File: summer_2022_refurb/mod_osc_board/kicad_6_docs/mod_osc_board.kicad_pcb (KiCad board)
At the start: 2 copper layers, 123.2 x 76.2 mm, 112 parts, among them J1 ext_port, J2 ribbon_board_port, J3 adsr_board_port, J4 vco_board_port, J5 vcf_board_port, J6 power_entry, SW101 SW_SPDT_MSM, SW201 alpha_SR2612F-0112, U201 SSI2130, U202 TL072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

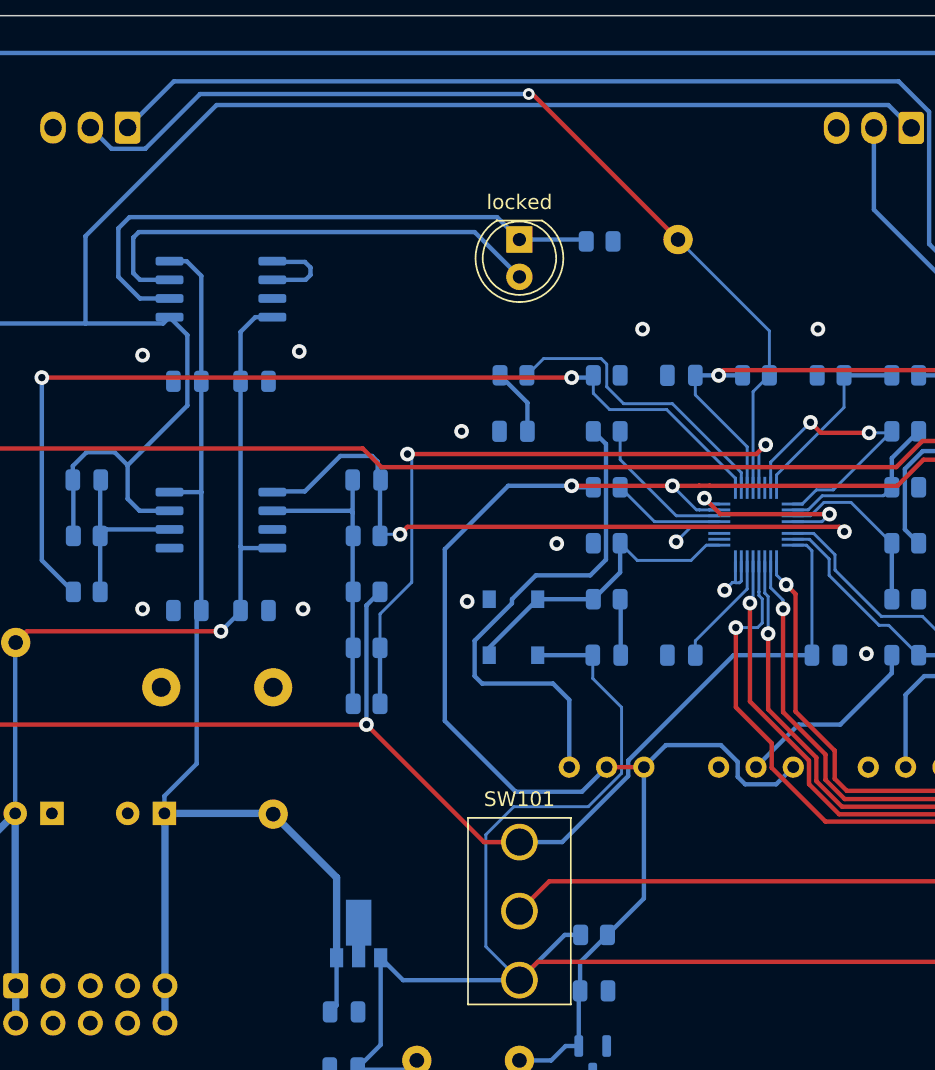
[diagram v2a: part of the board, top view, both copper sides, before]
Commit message: Buffer square, add saw polarity jumper
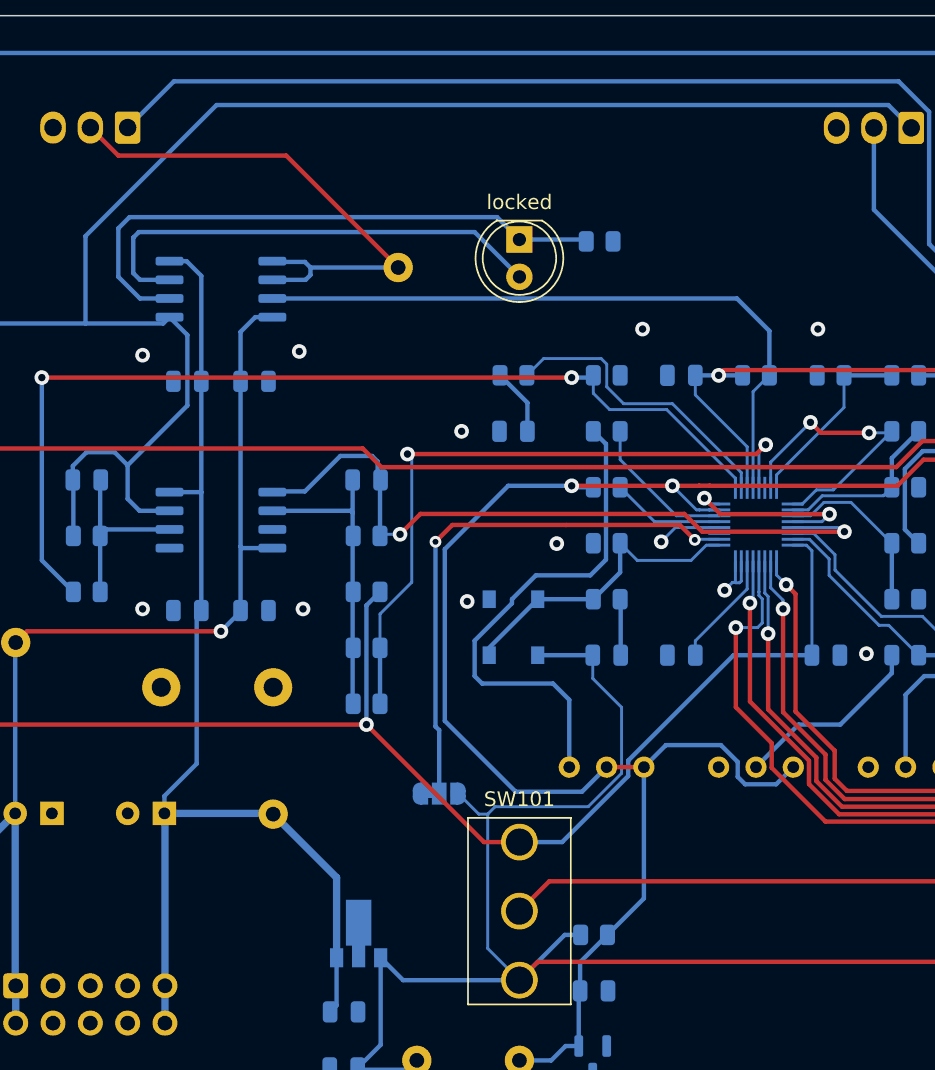
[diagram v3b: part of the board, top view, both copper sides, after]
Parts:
- added JP201: saw_pol, Jumper:SolderJumper-3_P1.3mm_Bridged12_RoundedPad1.0x1.5mm, B.Cu at (94.9, 91.1)
- added kibuzzard-62ACB089: G***, kibuzzard-62ACB089, B.Cu at (94.9, 93.2)
- moved TP101 19.1 mm to (92.1, 55.2)
- moved kibuzzard-62AC7DA9 19.1 mm to (92.1, 58.4)
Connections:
- net /VCO_core/DOWN_SAW renamed /VCO_core/INV_SAW
- J2 pad 2: /VCO_core/RAW_SQUARE_OUT -> /VCO_core/SQUARE_OUT
- R213 pad 1: /VCO_core/RAW_SQUARE_OUT -> Net-(R213-Pad1)
- TP101 pad 1: /VCO_core/RAW_SQUARE_OUT -> /VCO_core/SQUARE_OUT
- U201 pad 18: unconnected-(U201-Pad18) -> Net-(JP201-Pad2)
- U201 pad 28: /VCO_core/RAW_SQUARE_OUT -> Net-(R213-Pad1)
- U301 pad 1: Net-(U301-Pad1) -> /VCO_core/SQUARE_OUT
- U301 pad 2: Net-(U301-Pad1) -> /VCO_core/SQUARE_OUT
- U301 pad 3: GND -> Net-(R213-Pad1)
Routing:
- net /VCO_core/RAW_SQUARE_OUT: track 66.2 -> 0.00 mm, vias 1 -> 0
- net Net-(R213-Pad1): track 0.00 -> 45.9 mm
- net Net-(JP201-Pad2): track 0.00 -> 37.5 mm, vias 0 -> 2
- net /VCO_core/SQUARE_OUT: track 0.00 -> 36.9 mm
- net Net-(U301-Pad1): track 6.02 -> 0.00 mm
- net +5V: track 255.2 -> 258.5 mm
- net GND: track 7.53 -> 8.55 mm
- net /VCO_core/INV_SAW: track 49.1 -> 49.8 mm
